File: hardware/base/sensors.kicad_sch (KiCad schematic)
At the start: 11 parts, among them U2 FXOS8700CQR1, U3 MS5637-02BA03

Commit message: schematic complete unreviewed
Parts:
- removed R2: 10k, Resistor_SMD:R_0402_1005Metric, symbol Device:R_Small
- removed U2: FXOS8700CQR1, Package_LGA:LGA-16_3x3mm_P0.5mm_LayoutBorder3x5y, symbol bt_Sensor_Motion:FXOS8700CQR1
- removed U3: MS5637-02BA03, bt_Package_LGA:TE_MS563702BA03-50, symbol bt_Sensor_Environmental:MS5637-02BA03
- added C2: 4.7u, Capacitor_SMD:C_0603_1608Metric, symbol Device:C_Small
- added R9: 10k, Resistor_SMD:R_0402_1005Metric, symbol Device:R_Small
- added U10: LTR-329ALS-01, Package_LGA:VLGA-4_2x2.5mm_P1.65mm, symbol bt_Sensor_Environmental:LTR-329ALS-01
- added U5: FXOS8700CQR1, Package_LGA:LGA-16_3x3mm_P0.5mm_LayoutBorder3x5y, symbol bt_Sensor_Motion:FXOS8700CQR1
- added U6: MS5637-02BA03, bt_Package_LGA:TE_MS563702BA03-50, symbol bt_Sensor_Environmental:MS5637-02BA03
- C11: value 4.7u -> 0.1u; footprint Capacitor_SMD:C_0603_1608Metric -> Capacitor_SMD:C_0402_1005Metric; Voltage 25V -> 50V
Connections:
- net GND: now also C2.2, R9.2, U10.2 (GND), U5.10 (SA1/CS_B), U5.12 (GND), U5.13 (RSVD), U5.3 (RSVD), U5.5 (GND), U5.7 (SA0/MISO), U6.4 (GND)
- net SYS_I2C.SCL: now also U10.3 (SCL), U5.4 (SCL/SCLK), U6.3 (SCL)
- net SYS_I2C.SDA: now also U10.4 (SDA), U5.6 (SDA/MOSI), U6.2 (SDA)
- net VDD_AUX_3V3: now reaches C14.1
- net VDD_AUX_3V3: now also C11.1, C12.1, C15.1, R3.1, R4.1, C2.1, U10.1 (VDD), U5.1 (VDDIO), U5.14 (VDD), U6.1 (VDD)
- net at C16.1: now also U5.8 (CRST)
- removed net +3V3: C11.1, C12.1, C13.1, C15.1, R3.1, R4.1
- new net: R9.1, U5.16 (RST)
- new net: C13.1, U5.2 (BYP)
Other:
- moved on the sheet: R3, R4

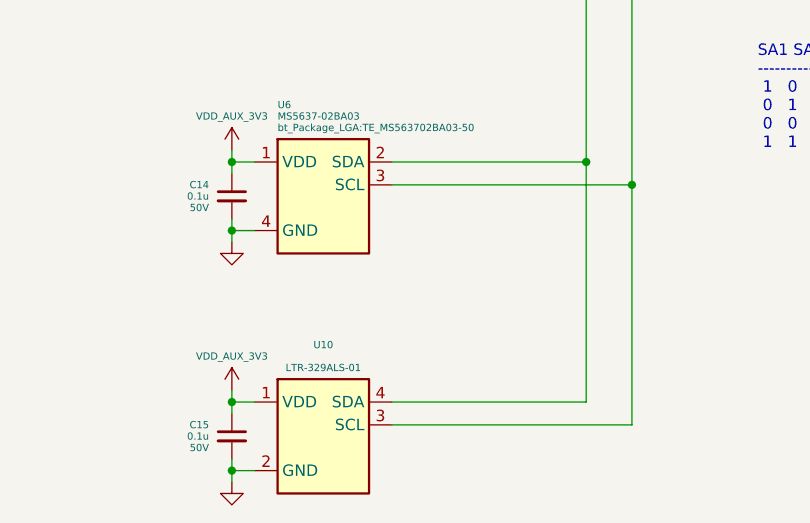
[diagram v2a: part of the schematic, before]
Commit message: split back out condensed board into lcdboard and base
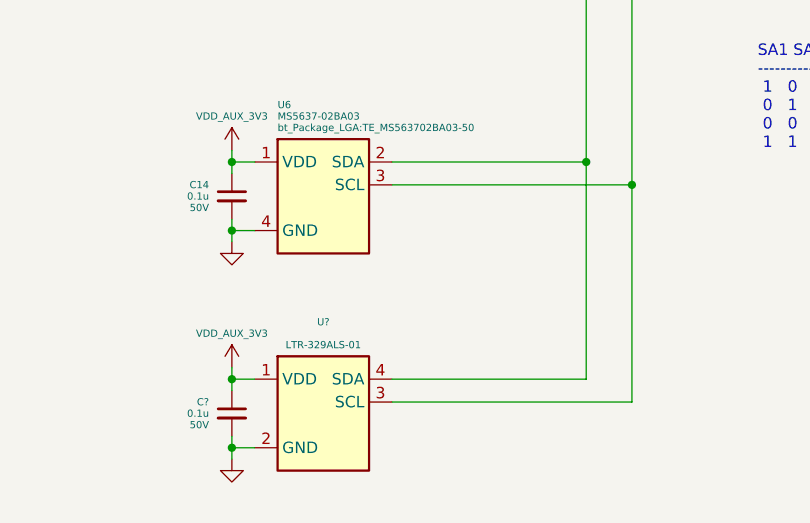
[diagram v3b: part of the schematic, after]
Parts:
- removed C15: 0.1u, Capacitor_SMD:C_0402_1005Metric, symbol Device:C_Small
- removed U10: LTR-329ALS-01, Package_LGA:VLGA-4_2x2.5mm_P1.65mm, symbol bt_Sensor_Environmental:LTR-329ALS-01
- added C?: 0.1u, Capacitor_SMD:C_0402_1005Metric, symbol Device:C_Small
- added U?: LTR-329ALS-01, Package_LGA:VLGA-4_2x2.5mm_P1.65mm, symbol bt_Sensor_Environmental:LTR-329ALS-01
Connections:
- net GND: now also C?.2, U?.2 (GND)
- net SYS_I2C.SCL: now also U?.3 (SCL)
- net SYS_I2C.SDA: now also U?.4 (SDA)
- net VDD_AUX_3V3: now also C?.1, U?.1 (VDD)

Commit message: completed layout for lcdboard prototype, may need to move b2b down for clearance on mainboard.
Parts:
- gave numbers to parts that had none: 2
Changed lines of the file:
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@@
   (symbol (lib_id "Device:C_Small") (at 74.93 144.78 0) (mirror y) (unit 1)
     (in_bom yes) (on_board yes)
-    (property "Reference" "C?" (id 0) (at 72.39 143.51 0)
+    (property "Reference" "C9" (id 0) (at 72.39 143.51 0)
       (effects (font (size 0.8 0.8)) (justify left))
     )
@@
   (symbol (lib_id "bt_Sensor_Environmental:LTR-329ALS-01") (at 85.09 143.51 0) (unit 1)
     (in_bom yes) (on_board yes) (fields_autoplaced)
-    (property "Reference" "U?" (id 0) (at 85.09 134.62 0)
+    (property "Reference" "U2" (id 0) (at 85.09 134.62 0)
       (effects (font (size 0.8 0.8)))
     )
@@
   (symbol (lib_id "power:GND") (at 74.93 149.86 0) (unit 1)
     (in_bom yes) (on_board yes) (fields_autoplaced)
-    (property "Reference" "#PWR?" (id 0) (at 74.93 156.21 0)
+    (property "Reference" "#PWR0108" (id 0) (at 74.93 156.21 0)
       (effects (font (size 1.27 1.27)) hide)
     )
@@
   (symbol (lib_id "bt_power:VDD_AUX_3V3") (at 74.93 139.7 0) (unit 1)
     (in_bom no) (on_board no) (fields_autoplaced)
-    (property "Reference" "#PWR?" (id 0) (at 75.4634 139.7 0)
-      (effects (font (size 1.27 1.27)) hide)
-    )
+    (property "Reference" "#PWR0106" (id 0) (at 75.4634 139.7 0)
+      (effects (font (size 1.27 1.27)) hide)
+    )

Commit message: layout
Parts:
- removed R3, R4: 4.7k, Resistor_SMD:R_0402_1005Metric, symbol Device:R_Small
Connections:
- net imu_reset: now reaches R9.1, U5.16 (RST)
- net imu_byp: now reaches C13.1, U5.2 (BYP)
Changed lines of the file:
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@@
   (junction (at 69.85 87.63) (diameter 0) (color 0 0 0 0)
-  )
-  (junction (at 114.3 58.42) (diameter 0) (color 0 0 0 0)
   )
   (junction (at 74.93 116.84) (diameter 0) (color 0 0 0 0)
@@
     (stroke (width 0) (type default) (color 0 0 0 0))
   )
-  (wire (pts (xy 114.3 58.42) (xy 114.3 59.69))
-    (stroke (width 0) (type default) (color 0 0 0 0))
-  )
   (wire (pts (xy 92.71 143.51) (xy 119.38 143.51))
     (stroke (width 0) (type default) (color 0 0 0 0))
   )
-  (wire (pts (xy 114.3 57.15) (xy 114.3 58.42))
-    (stroke (width 0) (type default) (color 0 0 0 0))
-  )
   (wire (pts (xy 96.52 74.93) (xy 97.79 74.93))
     (stroke (width 0) (type default) (color 0 0 0 0))
@@
     (stroke (width 0) (type default) (color 0 0 0 0))
   )
-  (wire (pts (xy 119.38 64.77) (xy 119.38 69.85))
-    (stroke (width 0) (type default) (color 0 0 0 0))
-  )
   (wire (pts (xy 43.18 87.63) (xy 50.8 87.63))
     (stroke (width 0) (type default) (color 0 0 0 0))
@@
     (stroke (width 0) (type default) (color 0 0 0 0))
   )
-  (wire (pts (xy 114.3 58.42) (xy 119.38 58.42))
-    (stroke (width 0) (type default) (color 0 0 0 0))
-  )
   (wire (pts (xy 114.3 67.31) (xy 114.3 116.84))
     (stroke (width 0) (type default) (color 0 0 0 0))
@@
     (stroke (width 0) (type default) (color 0 0 0 0))
   )
-  (wire (pts (xy 119.38 59.69) (xy 119.38 58.42))
-    (stroke (width 0) (type default) (color 0 0 0 0))
-  )
   (wire (pts (xy 96.52 87.63) (xy 97.79 87.63))
     (stroke (width 0) (type default) (color 0 0 0 0))
@@
   )
   (wire (pts (xy 74.93 123.19) (xy 74.93 124.46))
-    (stroke (width 0) (type default) (color 0 0 0 0))
-  )
-  (wire (pts (xy 114.3 64.77) (xy 114.3 67.31))
     (stroke (width 0) (type default) (color 0 0 0 0))
   )
@@
     (effects (font (size 1.27 1.27)) (justify left bottom))
   )
+  (label "imu_reset" (at 105.41 83.82 180)
+    (effects (font (size 0.8 0.8)) (justify right bottom))
+  )
+  (label "imu_byp" (at 66.04 73.66 0)
+    (effects (font (size 0.8 0.8)) (justify left bottom))
+  )
   (hierarchical_label "SYS_I2C{SDA SCL}" (shape bidirectional) (at 156.21 62.23 0)
     (effects (font (size 0.8 0.8)) (justify left))
-  )
-  (symbol (lib_id "Device:R_Small") (at 119.38 62.23 0) (unit 1)
-    (in_bom yes) (on_board yes)
-    (property "Reference" "R4" (id 0) (at 120.65 60.96 0)
-      (effects (font (size 0.8 0.8)) (justify left))
-    )
-    (property "Value" "4.7k" (id 1) (at 120.65 62.23 0)
-      (effects (font (size 0.8 0.8)) (justify left))
-    )
-    (property "Footprint" "Resistor_SMD:R_0402_1005Metric" (id 2) (at 119.38 62.23 0)
-      (effects (font (size 0.8 0.8)) hide)
-    )
-    (property "Datasheet" "~" (id 3) (at 119.38 62.23 0)
-      (effects (font (size 0.8 0.8)) hide)
-    )
-    (pin "1")
-    (pin "2")
   )
   (symbol (lib_id "Device:C_Small") (at 74.93 120.65 0) (mirror y) (unit 1)
@@
     (pin "9")
   )
-  (symbol (lib_id "Device:R_Small") (at 114.3 62.23 0) (unit 1)
-    (in_bom yes) (on_board yes)
-    (property "Reference" "R3" (id 0) (at 115.57 60.96 0)
-      (effects (font (size 0.8 0.8)) (justify left))
-    )
-    (property "Value" "4.7k" (id 1) (at 115.57 62.23 0)
-      (effects (font (size 0.8 0.8)) (justify left))
-    )
-    (property "Footprint" "Resistor_SMD:R_0402_1005Metric" (id 2) (at 114.3 62.23 0)
-      (effects (font (size 0.8 0.8)) hide)
-    )
-    (property "Datasheet" "~" (id 3) (at 114.3 62.23 0)
-      (effects (font (size 0.8 0.8)) hide)
-    )
-    (pin "1")
-    (pin "2")
-  )
   (symbol (lib_id "power:GND") (at 69.85 95.25 0) (unit 1)
     (in_bom yes) (on_board yes) (fields_autoplaced)
@@
     (pin "2")
   )
-  (symbol (lib_id "bt_power:VDD_AUX_3V3") (at 114.3 57.15 0) (unit 1)
-    (in_bom no) (on_board no) (fields_autoplaced)
-    (property "Reference" "#PWR0190" (id 0) (at 114.8334 57.15 0)
-      (effects (font (size 1.27 1.27)) hide)
-    )
-    (property "Value" "VDD_AUX_3V3" (id 1) (at 114.3 53.34 0)
-      (effects (font (size 0.8 0.8)))
-    )
-    (property "Footprint" "" (id 2) (at 114.8334 57.15 0)
-      (effects (font (size 1.27 1.27)) hide)
-    )
-    (property "Datasheet" "" (id 3) (at 114.8334 57.15 0)
-      (effects (font (size 1.27 1.27)) hide)
-    )
-    (pin "1")
-  )
   (symbol (lib_id "power:GND") (at 74.93 149.86 0) (unit 1)

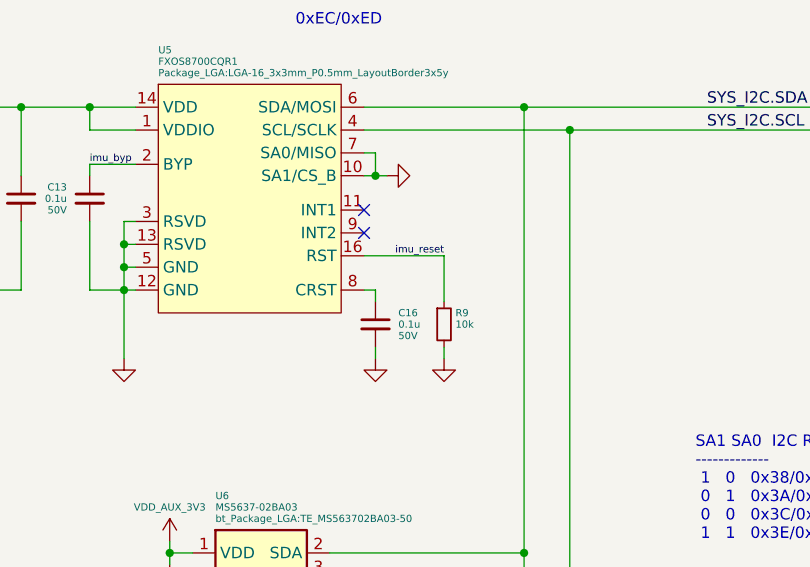
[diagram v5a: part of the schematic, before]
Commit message: more layout, optimising i2c
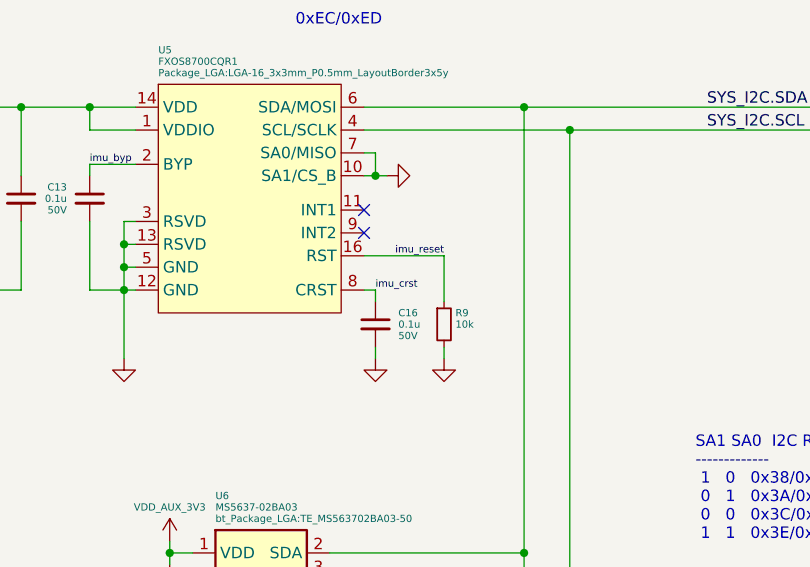
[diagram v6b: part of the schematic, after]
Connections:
- net imu_crst: now reaches C16.1, U5.8 (CRST)
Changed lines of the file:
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@@
     (effects (font (size 1.27 1.27)) (justify left bottom))
+  )
+  (label "imu_crst" (at 97.79 87.63 0)
+    (effects (font (size 0.8 0.8)) (justify left bottom))
   )
   (label "SYS_I2C.SDA" (at 134.62 67.31 0)

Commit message: layout complete, drc checks and tweaks to silkscreen, attempting geo reannotate
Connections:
- net SYS_I2C.SCL renamed AUX_I2C.SCL
- net SYS_I2C.SDA renamed AUX_I2C.SDA
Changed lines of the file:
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@@
     (effects (font (size 0.8 0.8)) (justify left bottom))
   )
-  (label "SYS_I2C.SDA" (at 134.62 67.31 0)
+  (label "AUX_I2C.SDA" (at 134.62 67.31 0)
     (effects (font (size 1.27 1.27)) (justify left bottom))
   )
-  (label "SYS_I2C.SCL" (at 134.62 69.85 0)
+  (label "AUX_I2C.SCL" (at 134.62 69.85 0)
     (effects (font (size 1.27 1.27)) (justify left bottom))
   )
@@
     (effects (font (size 0.8 0.8)) (justify left bottom))
   )
-  (hierarchical_label "SYS_I2C{SDA SCL}" (shape bidirectional) (at 156.21 62.23 0)
+  (hierarchical_label "AUX_I2C{SDA SCL}" (shape bidirectional) (at 156.21 62.23 0)
     (effects (font (size 0.8 0.8)) (justify left))
   )
